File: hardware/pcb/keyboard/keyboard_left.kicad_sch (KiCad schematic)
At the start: 10 parts, among them J1 SM04B-SRSS-TB, J2 TRRS PJ320D, J4 FH34SRJ-10S-0.5SH, SW29 SW_Push, U3 nRF52840_holyiot_18010, U5 DT1446-04S

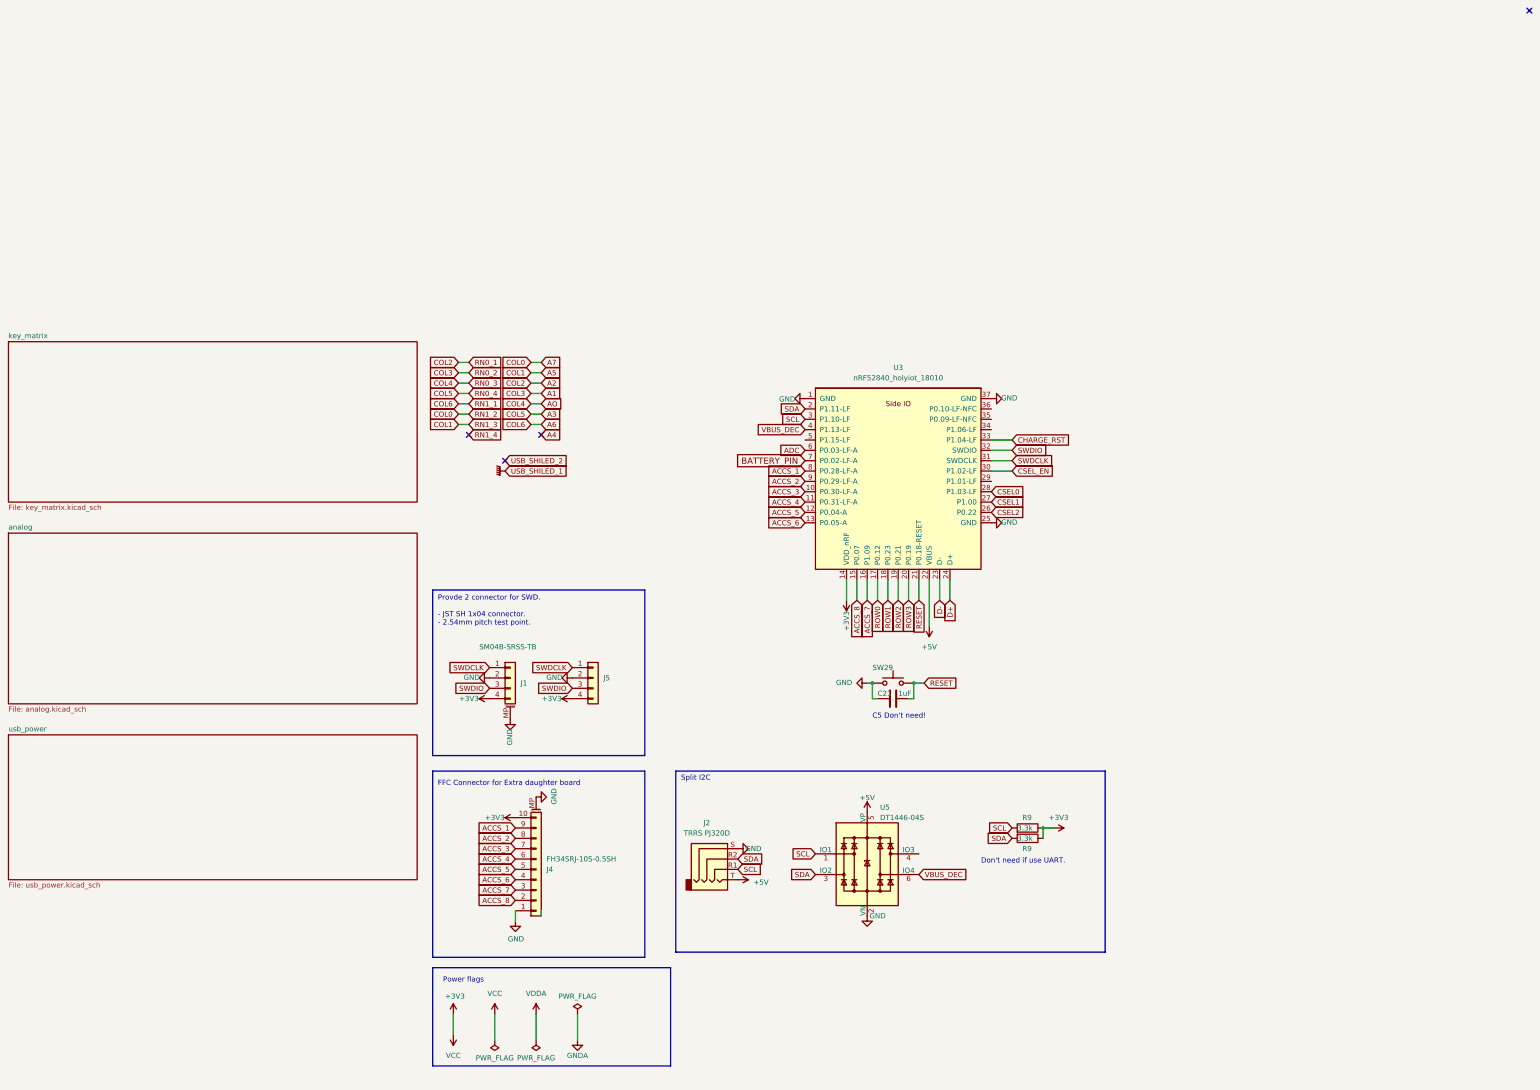
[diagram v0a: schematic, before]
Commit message: Init STM32G0 PCB
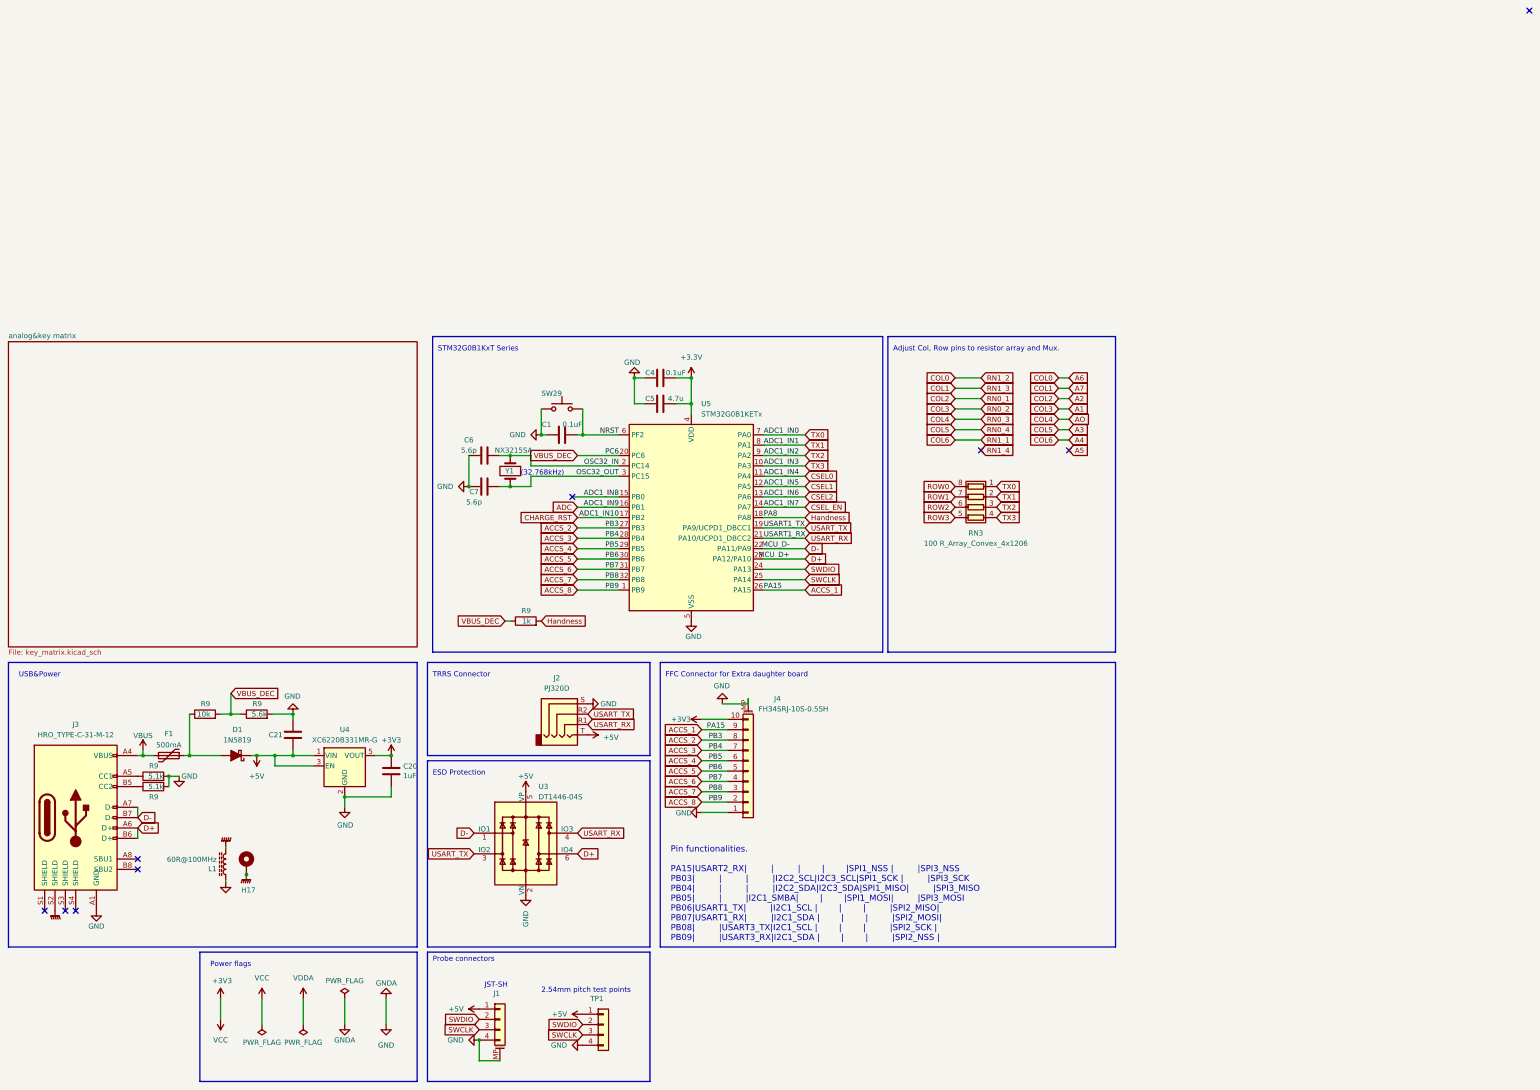
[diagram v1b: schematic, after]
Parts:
- removed J5: ~, ec_parts:PinHeader_1x04_P2.54mm_top_only, symbol Connector_Generic:Conn_01x04
- removed R9 (x2): 3.3k, PCM_Resistor_SMD_AKL:R_0603_1608Metric_Pad0.98x0.95mm, symbol Device:R
- removed U3: nRF52840_holyiot_18010, PCM_marbastlib-various:nRF52840_holyiot_18010_HS_simple, symbol PCM_marbastlib-various:nRF52840_holyiot_18010
- removed U5: DT1446-04S, PCM_Package_TO_SOT_SMD_AKL:SOT-363_SC-70-6_Handsoldering, symbol Power_Protection:SRV05-4
- added C1, C4: 0.1uF, PCM_Capacitor_SMD_AKL:C_0603_1608Metric_Pad1.05x0.95mm, symbol Device:C
- added C20: 1uF, PCM_Capacitor_SMD_AKL:C_0603_1608Metric_Pad1.05x0.95mm, symbol Device:C
- added C5: 4.7u, PCM_Capacitor_SMD_AKL:C_0603_1608Metric_Pad1.05x0.95mm, symbol Device:C
- added C6, C7: 5.6p, PCM_Capacitor_SMD_AKL:C_0603_1608Metric_Pad1.05x0.95mm, symbol Device:C
- added D1: 1N5819, PCM_Diode_SMD_AKL:D_SOD-323_HandSoldering, symbol PCM_Diode_Schottky_AKL:1N5818
- added F1: 500mA, PCM_Fuse_AKL:Fuse_1206_3216Metric, symbol Device:Polyfuse
- added H17: ~, ec_parts:PinHeader_1x01, symbol Mechanical:MountingHole_Pad
- added J3: HRO_TYPE-C-31-M-12, ec_parts:USB_C_Receptacle_HRO_TYPE-C-31-M-12, symbol ec_parts:USB_C_Receptacle_USB2.0
- added L1: 60R@100MHz, PCM_Inductor_SMD_AKL:L_1206_3216Metric, symbol Unified-Daughterboard-rescue:L_Core_Ferrite-Device
- added R9: 5.6k, PCM_Resistor_SMD_AKL:R_0603_1608Metric_Pad0.98x0.95mm, symbol Device:R
- added R9: 10k, PCM_Resistor_SMD_AKL:R_0603_1608Metric_Pad0.98x0.95mm, symbol Device:R
- added R9: 1k, PCM_Resistor_SMD_AKL:R_0603_1608Metric_Pad0.98x0.95mm, symbol Device:R
- added R9 (x2): 5.1k, PCM_Resistor_SMD_AKL:R_0603_1608Metric_Pad0.98x0.95mm, symbol Device:R
- added RN3: 100 R_Array_Convex_4x1206, PCM_Resistor_SMD_AKL:R_Array_Concave_4x0603, symbol PCM_Resistor_AKL:R_4x0612_Convex
- added TP1: ~, ec_parts:PinHeader_1x04_P2.54mm_test_pad, symbol Connector_Generic:Conn_01x04
- added U3: DT1446-04S, PCM_Package_TO_SOT_SMD_AKL:SOT-363_SC-70-6_Handsoldering, symbol Power_Protection:SRV05-4
- added U4: XC6220B331MR-G, PCM_Package_TO_SOT_SMD_AKL:SOT-23-5, symbol Regulator_Linear:AP2112K-3.3
- added U5: STM32G0B1KETx, PCM_Package_QFP_AKL:LQFP-32_7x7mm_P0.8mm, symbol MCU_ST_STM32G0:STM32G0B1KETx
- added Y1: NX3215SA, PCM_Crystal_AKL:Crystal_SMD_3215-2Pin_3.2x1.5mm, symbol Device:Crystal
- C21: footprint PCM_Capacitor_SMD_AKL:C_0603_1608Metric_Pad1.08x0.95mm -> PCM_Capacitor_SMD_AKL:C_0603_1608Metric_Pad1.05x0.95mm
- J2: value TRRS PJ320D -> PJ320D
- SW29: value SW_Push -> PTS845
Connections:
- net SWDCLK is gone; now on net +5V: J1.1 (Pin_1)
- net +3V3: now also C20.1, C4.1, C5.1, U4.5 (VOUT), U5.4 (VDD); no longer J1.4 (Pin_4)
- net +5V: now also C21.1, D1.1 (K), TP1.1 (Pin_1), U3.5 (VP), U4.1 (VIN), U4.3 (EN)
- net ACCS_1: now also U5.26 (PA15)
- net ACCS_2: now also U5.27 (PB3)
- net ACCS_3: now also U5.28 (PB4)
- net ACCS_4: now also U5.29 (PB5)
- net ACCS_5: now also U5.30 (PB6)
- net ACCS_6: now also U5.31 (PB7)
- net ACCS_7: now also U5.32 (PB8)
- net ACCS_8: now also U5.1 (PB9)
- net ADC: now also U5.16 (PB1)
- net CHARGE_RST: now also U5.17 (PB2)
- net CSEL0: now also U5.11 (PA4)
- net CSEL1: now also U5.12 (PA5)
- net CSEL2: now also U5.13 (PA6)
- net CSEL_EN: now also U5.14 (PA7)
- net D+: now also J3.A6 (D+), J3.B6 (D+), U3.6 (IO4), U5.23 (PA12/PA10)
- net D-: now also J3.A7 (D-), J3.B7 (D-), U3.1 (IO1), U5.22 (PA11/PA9)
- net GND: now also J1.4 (Pin_4), C1.1, C20.2, C4.2, C5.2, C6.1, C7.1, J3.A1 (GND), J3.A12 (GND), J3.B1 (GND), J3.B12 (GND), L1.1, R9.2, R9.2, R9.2, TP1.4 (Pin_4), U3.2 (VN), U4.2 (GND), U5.5 (VSS); no longer J1.2 (Pin_2)
- net GNDPWR: now also H17.1, J3.S2 (SHIELD), L1.2
- net ROW0: now also RN3.8 (R1.2)
- net ROW1: now also RN3.7 (R2.2)
- net ROW2: now also RN3.6 (R3.2)
- net ROW3: now also RN3.5 (R4.2)
- net SWDIO: now also J1.2 (Pin_2), TP1.2 (Pin_2), U5.24 (PA13); no longer J1.3 (Pin_3)
- net VBUS_DEC: now also R9.1, R9.1, R9.2, U5.20 (PC6)
- net RESET renamed NRST
- net NRST: now also C1.2, U5.6 (PF2); no longer C21.1
- net SCL renamed USART_RX
- net USART_RX: now also U3.4 (IO3), U5.21 (PA10/UCPD1_DBCC2)
- net SDA renamed USART_TX
- net USART_TX: now also U3.3 (IO2), U5.19 (PA9/UCPD1_DBCC1)
- new net: D1.2 (A), F1.1, R9.1
- new net: J3.A5 (CC1), R9.1
- new net: J3.B5 (CC2), R9.1
- new net ADC1_IN8: U5.15 (PB0)
- new net Handness: R9.2, U5.18 (PA8)
- new net OSC32_IN: C6.2, U5.2 (PC14), Y1.1
- new net OSC32_OUT: C7.2, U5.3 (PC15), Y1.2
- new net SWCLK: J1.3 (Pin_3), TP1.3 (Pin_3), U5.25 (PA14)
- new net TX0: RN3.1 (R1.1), U5.7 (PA0)
- new net TX1: RN3.2 (R2.1), U5.8 (PA1)
- new net TX2: RN3.3 (R3.1), U5.9 (PA2)
- new net TX3: RN3.4 (R4.1), U5.10 (PA3)
- new net VBUS: F1.2, J3.A4 (VBUS), J3.A9 (VBUS), J3.B4 (VBUS), J3.B9 (VBUS)
- no-connect marks 4 -> 9
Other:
- sheet key_matrix renamed analog&key matrix
- removed sheet analog
- removed sheet usb_power
- note added: "(32.768kHz)"
- note added: "2.54mm pitch test points"
- note added: "Adjust Col, Row pins to resistor array and Mux."
- note added: "ESD Protection"
- note added: "JST-SH"
- note added: "Pin functionalities. PA15|USART2_RX| | | | |SPI1_NSS | |SPI3_NSS PB03| | | |I2C2_SCL|I2C3_SCL|SPI1_SCK | |SPI3_SCK PB04| | | |I2C2_SDA|I2C3_SDA|SPI1_MISO| |SPI3_MISO PB05| | |I2C1_SMBA| | |SPI1_MOSI| |SPI3_MOSI PB06|USART1_TX| |I2C1_SCL | | | |SPI2_MISO| PB07|USART1_RX| |I2C1_SDA | | | |SPI2_MOSI| PB08| |USART3_TX|I2C1_SCL | | | |SPI2_SCK | PB09| |USART3_RX|I2C1_SDA | | | |SPI2_NSS |"
- note added: "Probe connectors"
- note added: "STM32G0B1KxT Series"
- note added: "TRRS Connector"
- note added: "USB&Power"
- note removed: "C5 Don't need!"
- note removed: "Don't need if use UART."
- note removed: "Provde 2 connector for SWD. - JST SH 1x04 connector. - 2.54mm pitch test point."
- note removed: "Split I2C"
- moved on the sheet: J2, J4

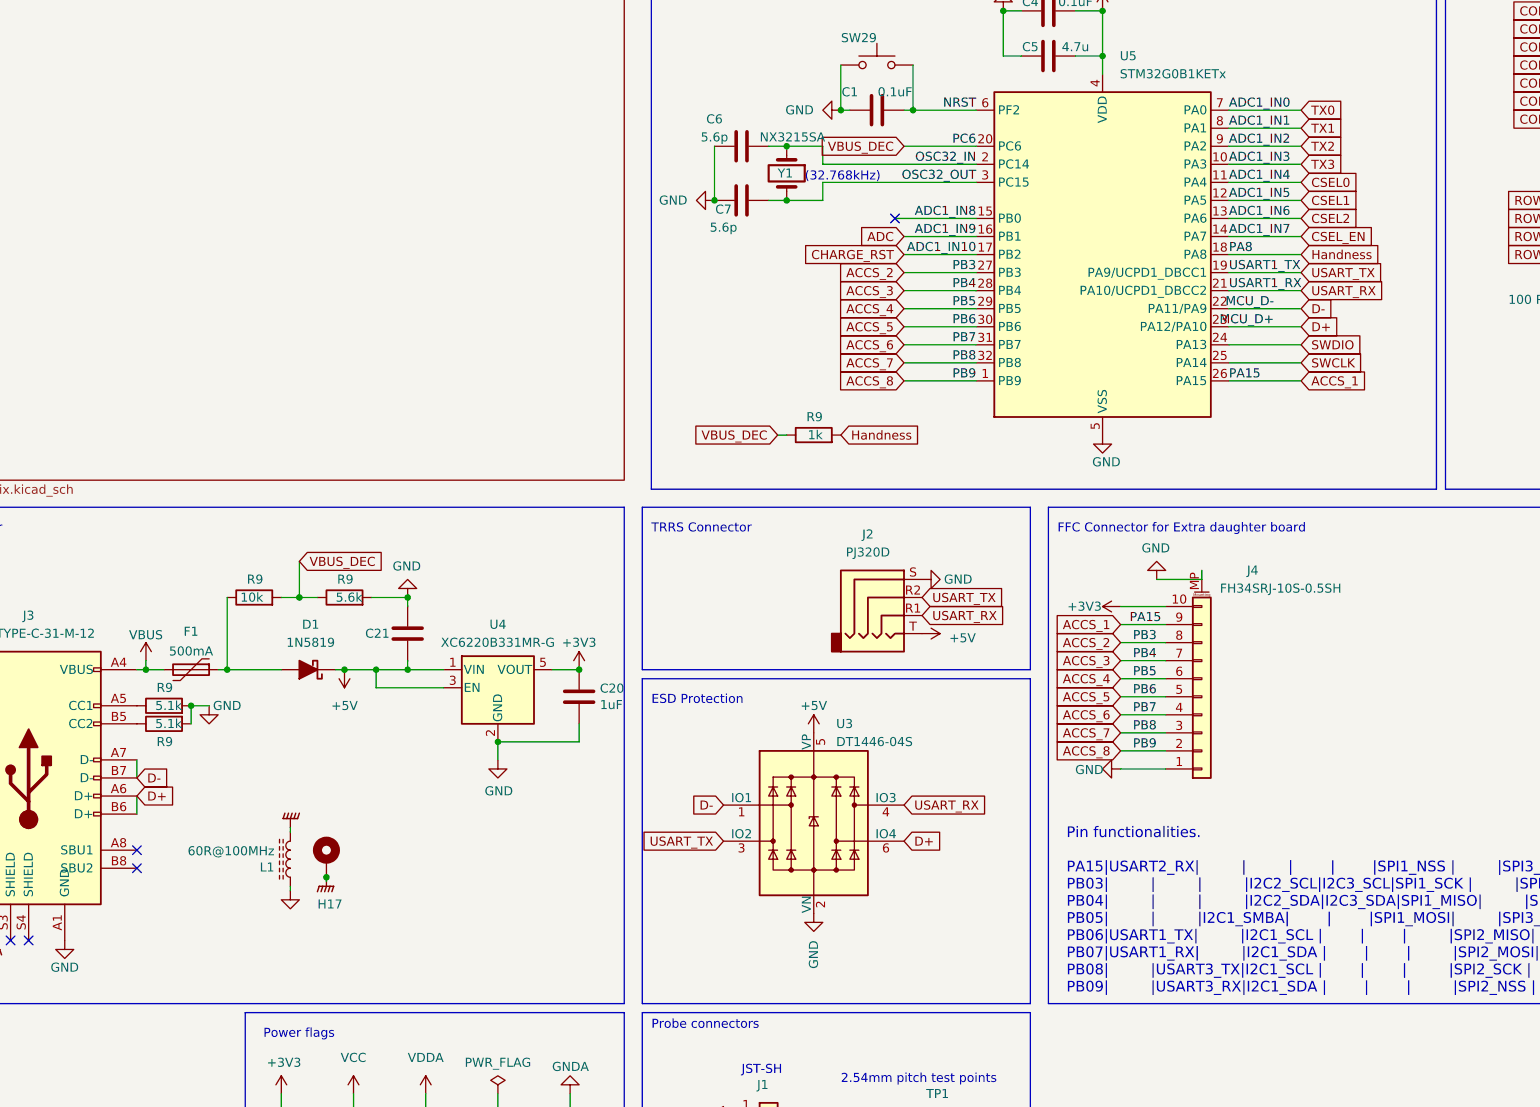
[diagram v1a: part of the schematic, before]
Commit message: Fix capacitor, resistor values
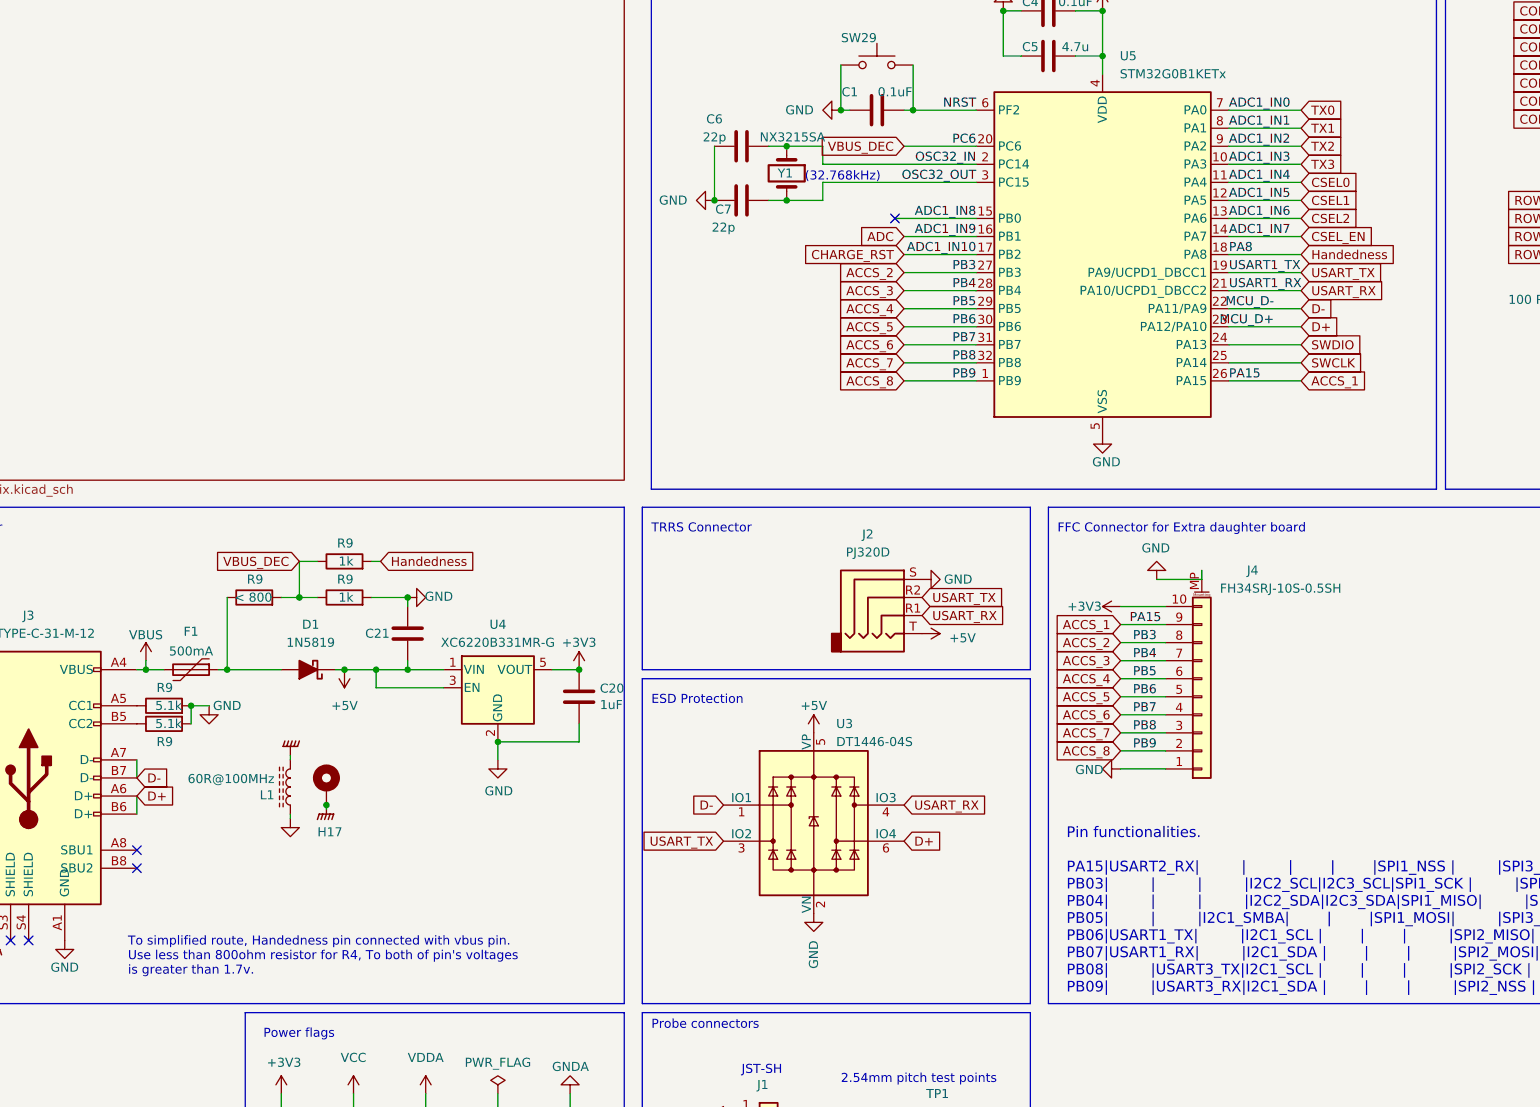
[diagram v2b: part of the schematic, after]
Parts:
- C6, C7: value 5.6p -> 22p
- R9: value 5.6k -> 1k
- R9: value 10k -> < 800
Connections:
- net Handness renamed Handedness
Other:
- note added: "To simplified route, Handedness pin connected with vbus pin. Use less than 800ohm resistor for R4, To both of pin's voltages is greater than 1.7v."
- title: (none) -> Corne EEC - Keyboard Left
- moved on the sheet: H17, L1
